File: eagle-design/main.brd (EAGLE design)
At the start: 132.1 x 33.3 mm, 18 parts, among them IC1 7805T

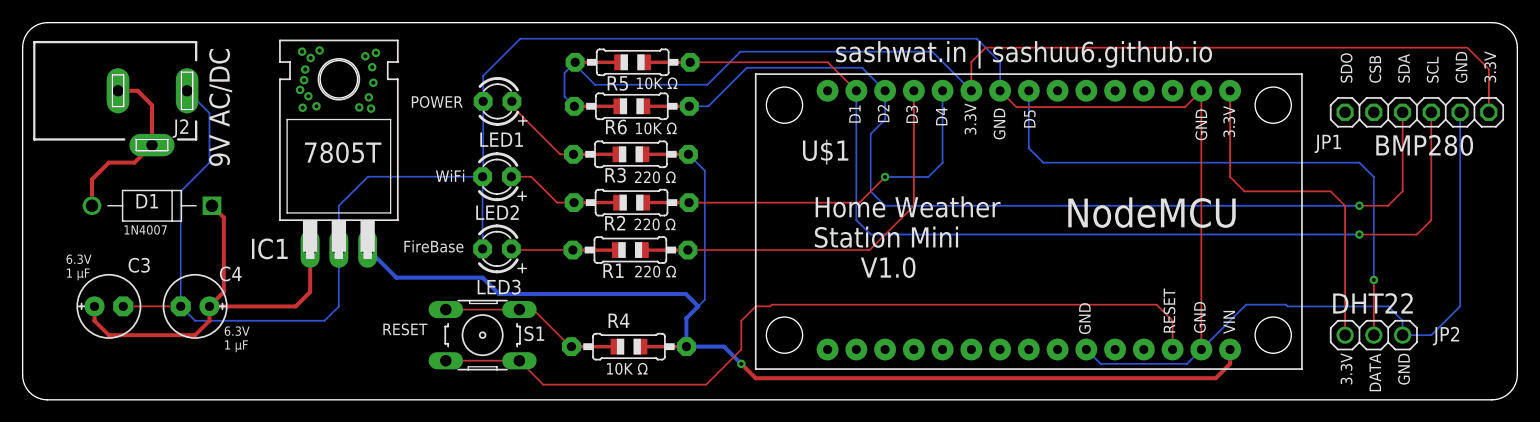
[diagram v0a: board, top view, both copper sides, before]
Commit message: Added support for reed switch and rain sensor
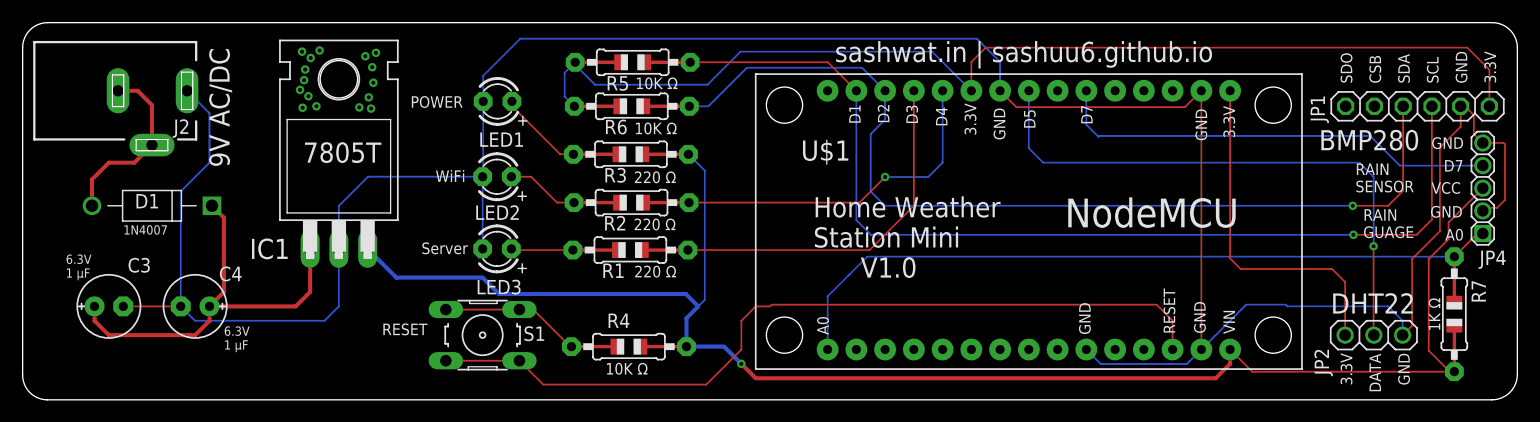
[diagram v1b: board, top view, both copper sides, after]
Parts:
- added JP4: (no value), pinhead:1_05X2MM
- added R7: 1K, adafruit:0805-THM
- moved JP1 0.54 mm to (125.1, 28.5)
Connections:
- new net N$30: IC1.3, JP4.3, R3.2, R4.2, R7.2, U$1.VIN
- new net N$31: JP4.1, R7.1, U$1.AD0
- net 0: now also JP4.2, JP4.5
- net N$32: now also JP4.4, U$1.D7; no longer IC1.3, R3.2, R4.2, U$1.VIN
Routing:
- net N$30: track 0.00 -> 140.9 mm, vias 0 -> 1
- net N$31: track 0.00 -> 64.9 mm
- net N$32: track 100.6 -> 39.6 mm, vias 1 -> 0
- net 0: track 227.0 -> 239.6 mm
- net N$8: track 88.5 -> 89.1 mm
- net N$7: track 84.0 -> 84.5 mm
- net N$14: track 96.6 -> 96.1 mm
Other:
- board text added: "1K Ω"
- board text added: "A0"
- board text added: "D7"
- board text added: "RAIN GUAGE"
- board text added: "RAIN SENSOR"
- board text added: "Server"
- board text added: "VCC"
- board text removed: "FireBase"

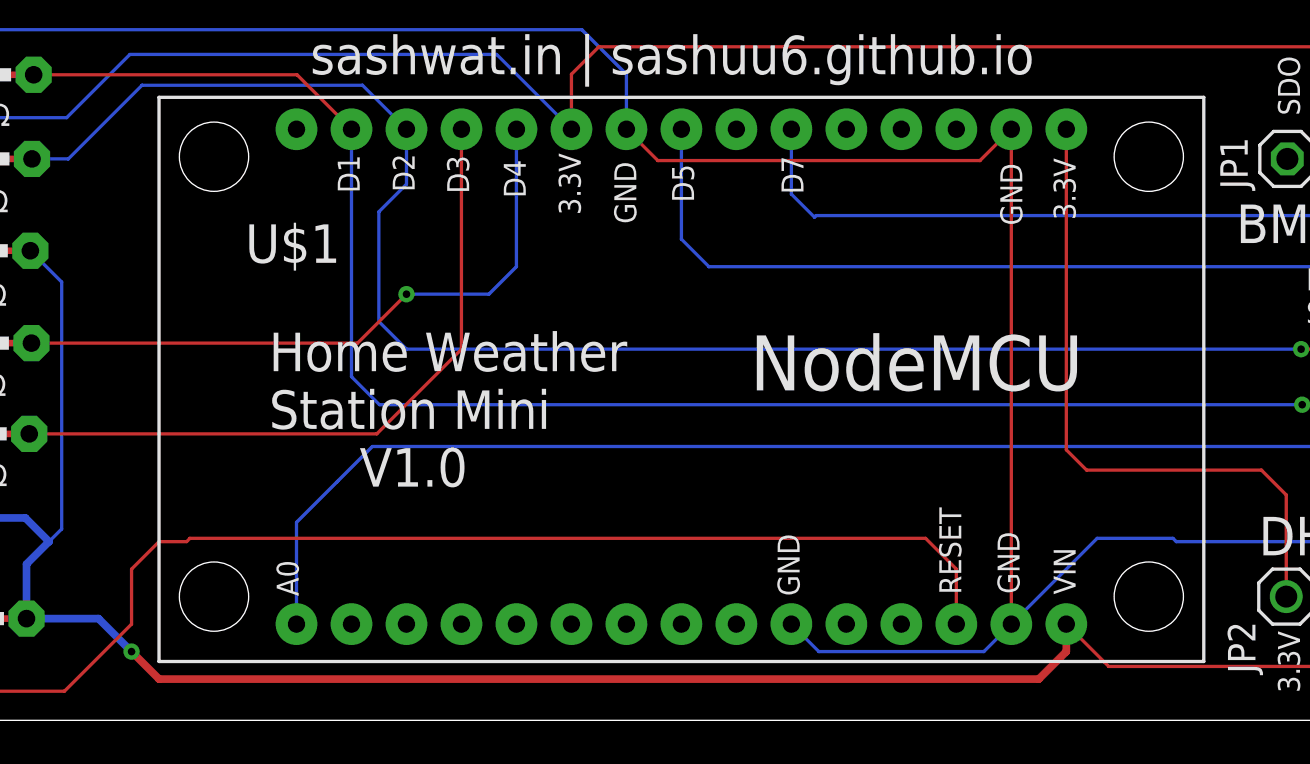
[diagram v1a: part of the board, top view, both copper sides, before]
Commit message: Micro SD Card reader added to eagle design ; New export images added
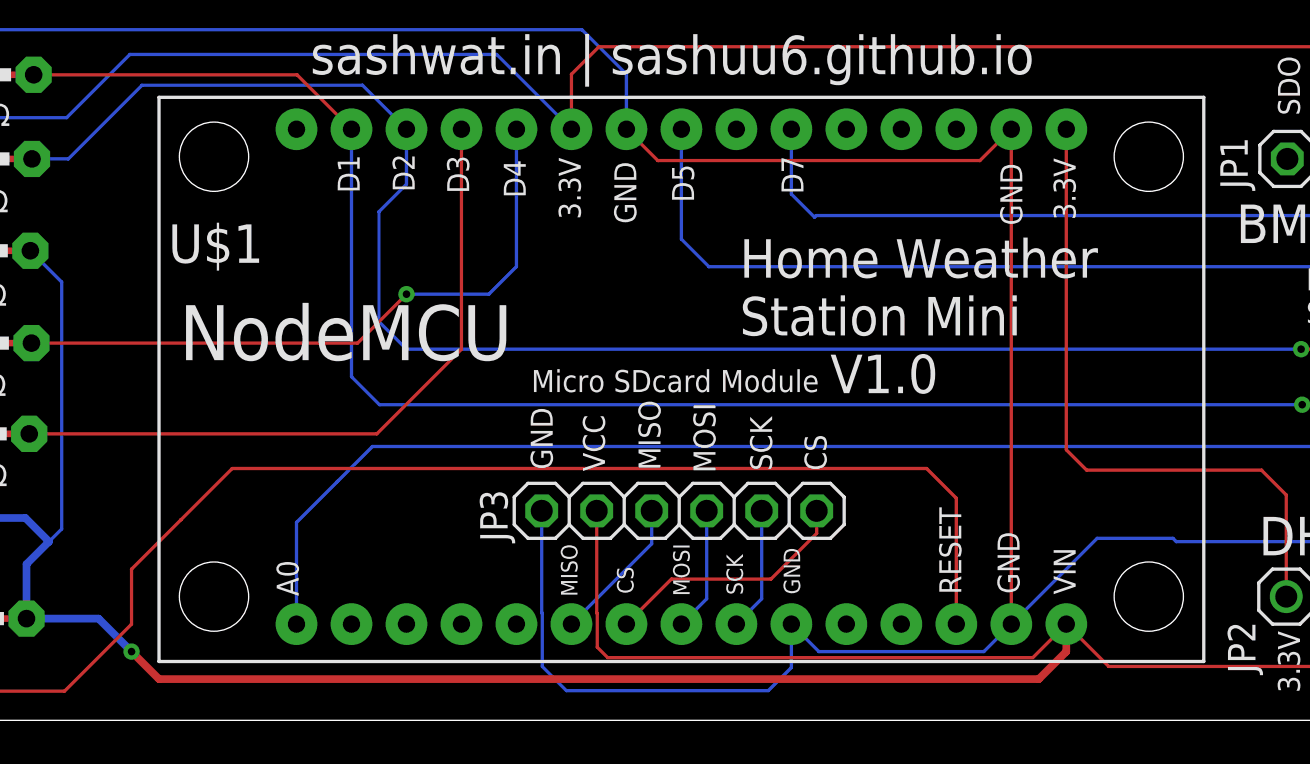
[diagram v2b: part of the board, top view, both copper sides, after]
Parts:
- added JP3: (no value), adafruit:1X06
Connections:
- new net N$33: JP3.4, U$1.SD0
- new net N$35: JP3.3, U$1.SD1
- new net N$36: JP3.5, U$1.CLK
- new net N$37: JP3.6, U$1.CMD
- net 0: now also JP3.1
- net N$30: now also JP3.2
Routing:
- net N$30: track 140.9 -> 169.8 mm
- net 0: track 239.6 -> 261.3 mm
- net N$37: track 0.00 -> 11.6 mm
- net N$35: track 0.00 -> 6.77 mm
- net N$36: track 0.00 -> 5.72 mm
- net N$33: track 0.00 -> 5.72 mm
- net N$11: track 72.6 -> 77.2 mm
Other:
- board text added: "CS"
- board text added: "MISO"
- board text added: "MOSI"
- board text added: "Micro SDcard Module"
- board text added: "SCK"
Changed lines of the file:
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@@
 <wire x1="131.7496" y1="35.865" x2="4.115" y2="35.865" width="0" layer="20"/>
 <wire x1="4.115" y1="35.865" x2="1.905" y2="33.655" width="0" layer="20" curve="90"/>
-<text x="71.755" y="13.335" size="1.778" layer="21">Home Weather
+<text x="93.4974" y="17.653" size="1.778" layer="21">Home Weather
 Station Mini
       V1.0</text>
@@
 <text x="116.4336" y="24.5872" size="1.778" layer="21">BMP280</text>
 <text x="117.475" y="10.16" size="1.778" layer="21">DHT22</text>
-<text x="93.98" y="17.78" size="2.54" layer="21">NodeMCU</text>
+<text x="67.6148" y="19.177" size="2.54" layer="21">NodeMCU</text>
 <text x="124.46" y="3.81" size="1.016" layer="21" rot="R90">GND</text>
 <text x="121.92" y="3.175" size="1.016" layer="21" rot="R90">DATA</text>
@@
 <text x="81.0006" y="26.8732" size="1.016" layer="21" rot="R90">D3</text>
 <text x="83.6168" y="26.67" size="1.016" layer="21" rot="R90">D4</text>
-<text x="86.1568" y="25.8826" size="1.016" layer="21" rot="R90">3.3V</text>
+<text x="86.1568" y="25.6794" size="1.016" layer="21" rot="R90">3.3V</text>
 <text x="88.7222" y="25.4762" size="1.016" layer="21" rot="R90">GND</text>
 <text x="91.3892" y="26.4668" size="1.016" layer="21" rot="R90">D5</text>
 <text x="106.553" y="25.4" size="1.016" layer="21" rot="R90">GND</text>
 <text x="109.0168" y="25.654" size="1.016" layer="21" rot="R90">3.3V</text>
-<text x="96.266" y="8.2804" size="1.016" layer="21" rot="R90">GND</text>
+<text x="96.2914" y="8.3566" size="0.762" layer="21" rot="R90">GND</text>
 <text x="106.426" y="8.382" size="1.016" layer="21" rot="R90">GND</text>
 <text x="103.7336" y="8.3566" size="1.016" layer="21" rot="R90">RESET</text>
@@
 <text x="119.6594" y="20.8788" size="1.016" layer="21">RAIN
 SENSOR</text>
+<text x="93.6498" y="8.3312" size="0.762" layer="21" rot="R90">SCK</text>
+<text x="91.186" y="8.2804" size="0.762" layer="21" rot="R90">MOSI</text>
+<text x="88.5952" y="8.382" size="0.762" layer="21" rot="R90">CS</text>
+<text x="86.0044" y="8.255" size="0.762" layer="21" rot="R90">MISO</text>
+<text x="84.8614" y="14.1224" size="1.016" layer="21" rot="R90">GND</text>
+<text x="87.2744" y="14.0462" size="1.016" layer="21" rot="R90">VCC</text>
+<text x="89.8398" y="14.097" size="1.016" layer="21" rot="R90">MISO</text>
+<text x="92.3798" y="13.97" size="1.016" layer="21" rot="R90">MOSI</text>
+<text x="94.996" y="14.0716" size="1.016" layer="21" rot="R90">SCK</text>
+<text x="97.5106" y="14.0716" size="1.016" layer="21" rot="R90">CS</text>
+<text x="83.8708" y="17.7038" size="1.016" layer="21">Micro SDcard Module</text>
 </plain>
 <attributes>
@@
 </element>
 <element name="U$1" library="ESP12E_DEVKIT" package="ESP12E_DEVKIT" value="ESP12E_DEVKIT" x="90.805" y="18.415" smashed="yes" rot="R90">
-<attribute name="NAME" x="75.057" y="25.4508" size="1.778" layer="25" rot="R180"/>
+<attribute name="NAME" x="71.501" y="25.4508" size="1.778" layer="25" rot="R180"/>
 <attribute name="VALUE" x="109.855" y="25.4" size="1.778" layer="27" rot="R180"/>
 </element>
@@
 <attribute name="POPULARITY" value="0" x="130.9116" y="21.2344" size="1.778" layer="27" rot="R90" display="off"/>
 <attribute name="VALUE" x="133.6616" y="16.4844" size="1.27" layer="27" rot="R90"/>
+</element>
+<element name="JP3" library="adafruit" package="1X06" value="" x="90.7034" y="12.2174" smashed="yes">
+<attribute name="NAME" x="82.7786" y="10.795" size="1.27" layer="25" ratio="10" rot="R90"/>
+<attribute name="VALUE" x="83.0834" y="9.0424" size="1.27" layer="27"/>
 </element>
 </elements>
@@
 <wire x1="127.127" y1="17.4498" x2="124.6632" y2="14.986" width="0.1524" layer="1"/>
 <wire x1="124.6632" y1="14.986" x2="124.6632" y2="9.0932" width="0.1524" layer="1"/>
+<contactref element="JP3" pad="1"/>
+<wire x1="84.3534" y1="12.2174" x2="84.3534" y2="7.50489375" width="0.1524" layer="16"/>
+<wire x1="84.3534" y1="7.50489375" x2="84.3788" y2="7.47949375" width="0.1524" layer="16"/>
+<wire x1="84.3788" y1="5.0292" x2="85.4964" y2="3.9116" width="0.1524" layer="16"/>
+<wire x1="84.3788" y1="7.47949375" x2="84.3788" y2="5.0292" width="0.1524" layer="16"/>
+<wire x1="85.4964" y1="3.9116" x2="94.8182" y2="3.9116" width="0.1524" layer="16"/>
+<wire x1="95.885" y1="4.9784" x2="95.885" y2="6.985" width="0.1524" layer="16"/>
+<wire x1="94.8182" y1="3.9116" x2="95.885" y2="4.9784" width="0.1524" layer="16"/>
 </signal>
 <signal name="N$1">
@@
 <contactref element="U$1" pad="RST"/>
 <wire x1="39.2938" y1="5.9944" x2="45.7962" y2="5.9944" width="0.1524" layer="1"/>
-<wire x1="103.505" y1="6.985" x2="103.505" y2="9.525" width="0.1524" layer="1"/>
-<wire x1="68.09985" y1="10.9472" x2="67.94765" y2="10.795" width="0.1524" layer="1"/>
-<wire x1="67.94765" y1="10.795" x2="66.675" y2="10.795" width="0.1524" layer="1"/>
-<wire x1="66.675" y1="10.795" x2="65.405" y2="9.525" width="0.1524" layer="1"/>
+<wire x1="103.505" y1="6.985" x2="103.505" y2="12.8016" width="0.1524" layer="1"/>
+<wire x1="70.05565" y1="14.173" x2="67.69365" y2="11.811" width="0.1524" layer="1"/>
+<wire x1="67.69365" y1="11.811" x2="67.691" y2="11.811" width="0.1524" layer="1"/>
+<wire x1="67.691" y1="11.811" x2="65.405" y2="9.525" width="0.1524" layer="1"/>
 <wire x1="65.405" y1="9.525" x2="65.405" y2="6.985" width="0.1524" layer="1"/>
 <wire x1="65.405" y1="6.985" x2="62.3062" y2="3.8862" width="0.1524" layer="1"/>
 <wire x1="62.3062" y1="3.8862" x2="47.9044" y2="3.8862" width="0.1524" layer="1"/>
 <wire x1="47.9044" y1="3.8862" x2="45.7962" y2="5.9944" width="0.1524" layer="1"/>
-<wire x1="103.505" y1="9.525" x2="102.0828" y2="10.9472" width="0.1524" layer="1"/>
-<wire x1="102.0828" y1="10.9472" x2="68.09985" y2="10.9472" width="0.1524" layer="1"/>
+<wire x1="103.505" y1="12.8016" x2="102.1336" y2="14.173" width="0.1524" layer="1"/>
+<wire x1="102.1336" y1="14.173" x2="70.05565" y2="14.173" width="0.1524" layer="1"/>
 </signal>
 <signal name="N$13">
@@
 <wire x1="128.397" y1="5.0292" x2="110.5408" y2="5.0292" width="0.1524" layer="1"/>
 <wire x1="110.5408" y1="5.0292" x2="108.585" y2="6.985" width="0.1524" layer="1"/>
+<contactref element="JP3" pad="2"/>
+<wire x1="86.8934" y1="12.2174" x2="86.8934" y2="7.50489375" width="0.1524" layer="1"/>
+<wire x1="86.8934" y1="7.50489375" x2="86.9188" y2="7.47949375" width="0.1524" layer="1"/>
+<wire x1="86.9188" y1="7.47949375" x2="86.9188" y2="5.9182" width="0.1524" layer="1"/>
+<wire x1="86.9188" y1="5.9182" x2="87.4014" y2="5.4356" width="0.1524" layer="1"/>
+<wire x1="107.0356" y1="5.4356" x2="108.585" y2="6.985" width="0.1524" layer="1"/>
+<wire x1="87.4014" y1="5.4356" x2="107.0356" y2="5.4356" width="0.1524" layer="1"/>
 </signal>
 <signal name="N$32">
@@
 <wire x1="117.602" y1="14.097" x2="118.745" y2="12.954" width="0.1524" layer="1"/>
 </signal>
+<signal name="N$35">
+<contactref element="U$1" pad="SD1"/>
+<contactref element="JP3" pad="3"/>
+<wire x1="85.725" y1="6.985" x2="89.4334" y2="10.6934" width="0.1524" layer="16"/>
+<wire x1="89.4334" y1="10.6934" x2="89.4334" y2="12.2174" width="0.1524" layer="16"/>
+</signal>
+<signal name="N$33">
+<contactref element="U$1" pad="SD0"/>
+<contactref element="JP3" pad="4"/>
+<wire x1="90.805" y1="6.985" x2="91.9734" y2="8.1534" width="0.1524" layer="16"/>
+<wire x1="91.9734" y1="8.1534" x2="91.9734" y2="12.2174" width="0.1524" layer="16"/>
+</signal>
+<signal name="N$36">
+<contactref element="U$1" pad="CLK"/>
+<contactref element="JP3" pad="5"/>
+<wire x1="93.345" y1="6.985" x2="94.5134" y2="8.1534" width="0.1524" layer="16"/>
+<wire x1="94.5134" y1="8.1534" x2="94.5134" y2="12.2174" width="0.1524" layer="16"/>
+</signal>
+<signal name="N$37">
+<contactref element="U$1" pad="CMD"/>
+<contactref element="JP3" pad="6"/>
+<wire x1="88.265" y1="6.985" x2="90.3478" y2="9.0678" width="0.1524" layer="1"/>
+<wire x1="90.3478" y1="9.0678" x2="94.9452" y2="9.0678" width="0.1524" layer="1"/>
+<wire x1="94.9452" y1="9.0678" x2="97.0534" y2="11.176" width="0.1524" layer="1"/>
+<wire x1="97.0534" y1="11.176" x2="97.0534" y2="12.2174" width="0.1524" layer="1"/>
+</signal>
 </signals>
